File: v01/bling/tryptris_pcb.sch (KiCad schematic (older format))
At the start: 131 parts, among them J1 USB_C_Receptacle_USB2.0, J2 I2C-L, J3 I2C-R, SW1 Reset, U1 ATmega32U4-AU, U2 MCP23017_SO, Y1 16Mhz

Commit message: Use freeform routing to get USB ports in a better position.
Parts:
- J1, J2, J3: footprint Type-C:USB_C_GCT_USB4085 -> Connector_USB:USB_C_Receptacle_HRO_TYPE-C-31-M-12
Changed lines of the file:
@@
 F 0 "J1" H 5207 2517 50  0000 C CNN
 F 1 "USB_C_Receptacle_USB2.0" H 5207 2426 50  0000 C CNN
-F 2 "Type-C:USB_C_GCT_USB4085" H 5250 1650 50  0001 C CNN
+F 2 "Connector_USB:USB_C_Receptacle_HRO_TYPE-C-31-M-12" H 5250 1650 50  0001 C CNN
 F 3 "https://www.usb.org/sites/default/files/documents/usb_type-c.zip" H 5250 1650 50  0001 C CNN
 	1    5100 1650
@@
 F 0 "J2" H 5357 5917 50  0000 C CNN
 F 1 "I2C-L" H 5357 5826 50  0000 C CNN
-F 2 "Type-C:USB_C_GCT_USB4085" H 5400 5050 50  0001 C CNN
+F 2 "Connector_USB:USB_C_Receptacle_HRO_TYPE-C-31-M-12" H 5400 5050 50  0001 C CNN
 F 3 "https://www.usb.org/sites/default/files/documents/usb_type-c.zip" H 5400 5050 50  0001 C CNN
 	1    5250 5050
@@
 F 0 "J3" H 4907 8217 50  0000 C CNN
 F 1 "I2C-R" H 4907 8126 50  0000 C CNN
-F 2 "Type-C:USB_C_GCT_USB4085" H 4950 7350 50  0001 C CNN
+F 2 "Connector_USB:USB_C_Receptacle_HRO_TYPE-C-31-M-12" H 4950 7350 50  0001 C CNN
 F 3 "https://www.usb.org/sites/default/files/documents/usb_type-c.zip" H 4950 7350 50  0001 C CNN
 	1    4800 7350

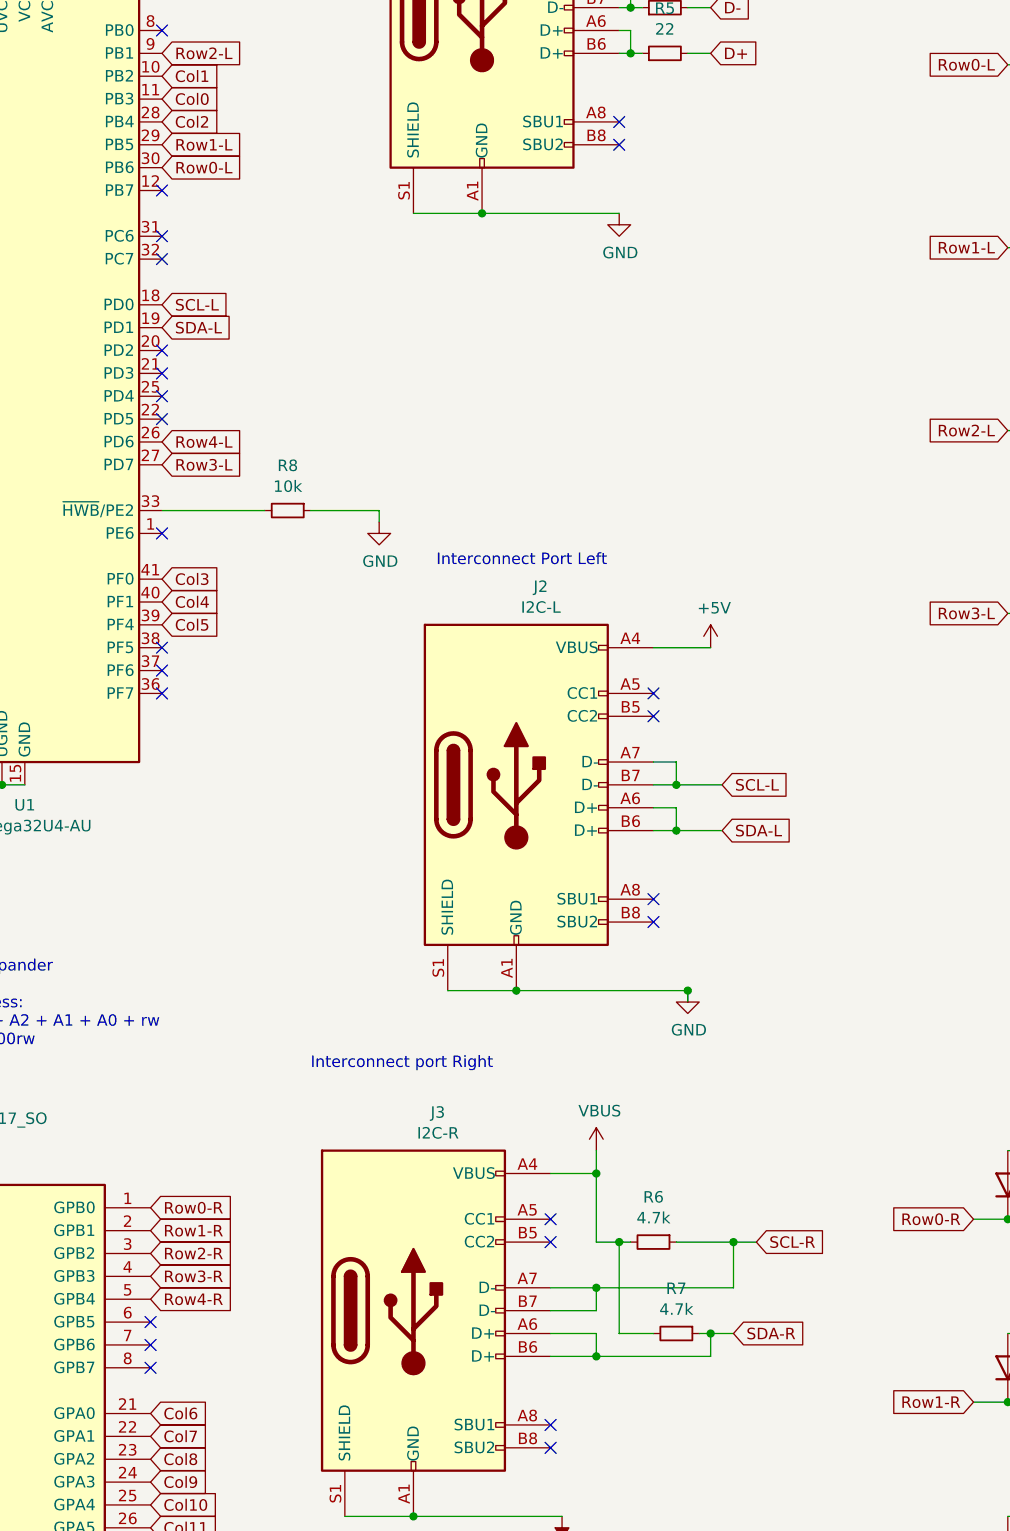
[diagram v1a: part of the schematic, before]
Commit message: Move I2C resistors to the left side for bling
This should ensure that the LED drivers on the left side work correctly
when the right side is not plugged in.
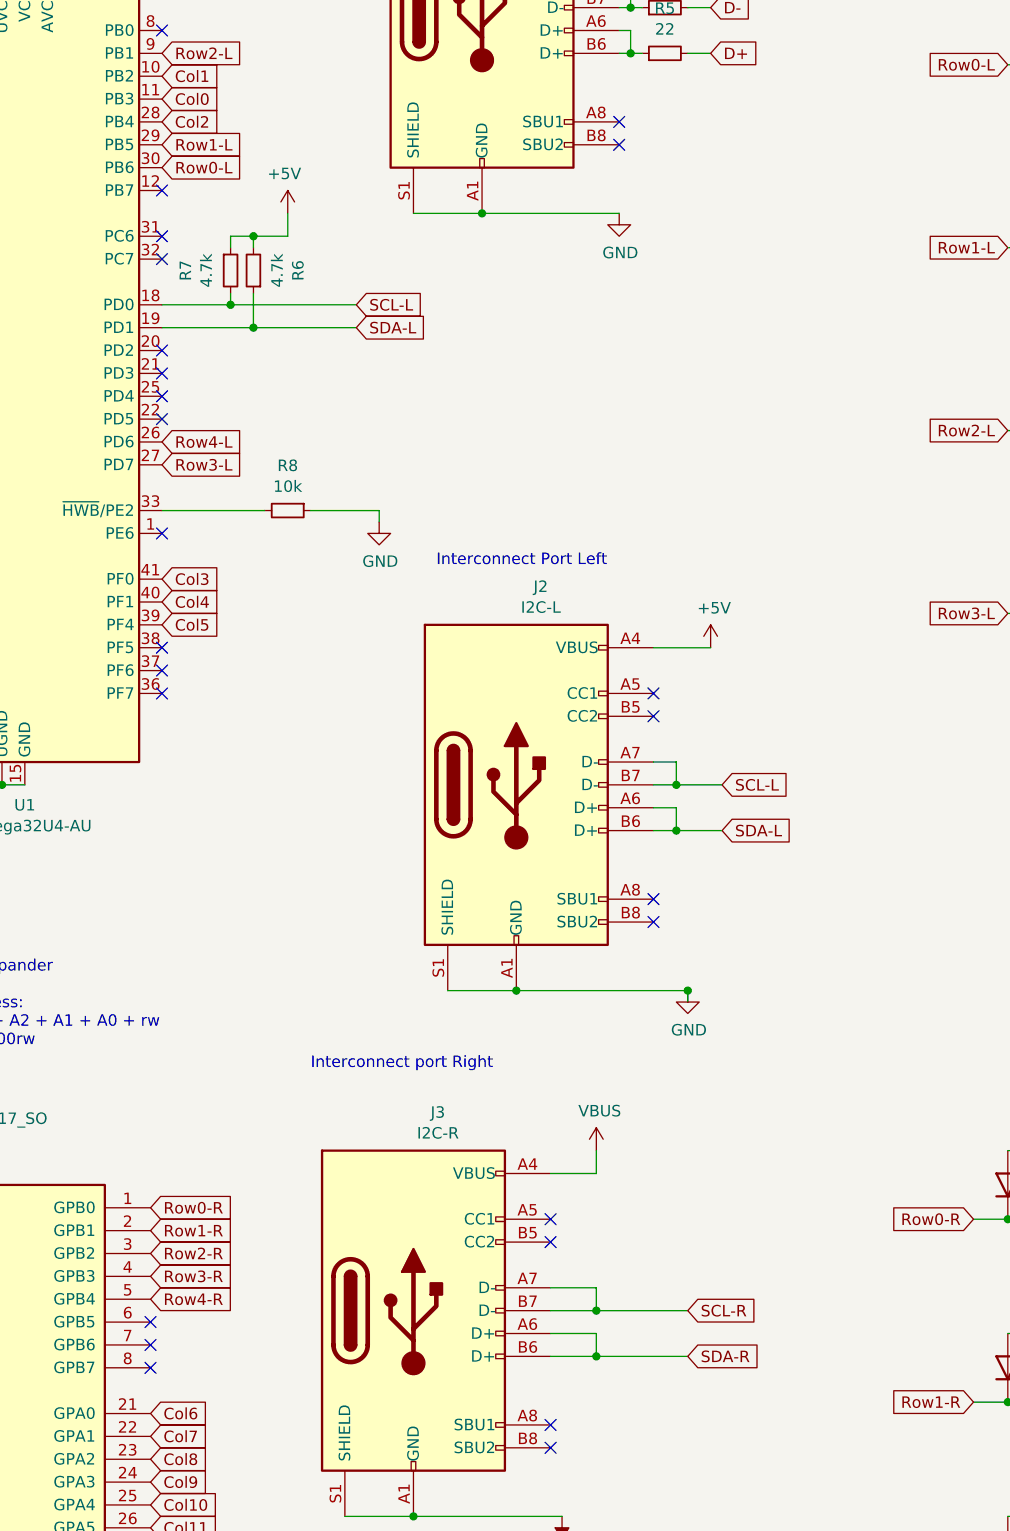
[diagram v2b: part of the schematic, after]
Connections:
- net +5V: now also R6.2, R7.1
- net SCL-L: now also R7.2
- net SCL-R: no longer R6.1
- net SDA-L: now also R6.1
- net SDA-R: no longer R7.1
- net VBUS: no longer R6.2, R7.2
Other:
- moved on the sheet: R6, R7
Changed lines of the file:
@@
 Text GLabel 2250 7000 0    50   Input ~ 0
 SCL-R
-Text GLabel 3700 3050 2    50   Input ~ 0
+Text GLabel 4550 3050 2    50   Input ~ 0
 SDA-L
-Text GLabel 3700 2950 2    50   Input ~ 0
+Text GLabel 4550 2950 2    50   Input ~ 0
 SCL-L
 Text Notes 4350 6300 0    50   ~ 0
@@
 Wire Wire Line
 	5600 6750 5600 6650
-Wire Wire Line
-	5600 7050 5700 7050
-Wire Wire Line
-	6200 7050 6300 7050
-Connection ~ 6200 7050
-Wire Wire Line
-	5950 7050 6200 7050
 $Comp
 L Device:R_Small R6
 U 1 1 615E83A9
-P 5850 7050
-F 0 "R6" V 5654 7050 50  0000 C CNN
-F 1 "4.7k" V 5745 7050 50  0000 C CNN
-F 2 "Resistor_SMD:R_0805_2012Metric" H 5850 7050 50  0001 C CNN
-F 3 "~" H 5850 7050 50  0001 C CNN
-	1    5850 7050
-	0    1    1    0
-$EndComp
-Text GLabel 6300 7050 2    50   Input ~ 0
+P 4100 2800
+F 0 "R6" V 3904 2800 50  0000 C CNN
+F 1 "4.7k" V 3995 2800 50  0000 C CNN
+F 2 "Resistor_SMD:R_0805_2012Metric" H 4100 2800 50  0001 C CNN
+F 3 "~" H 4100 2800 50  0001 C CNN
+	1    4100 2800
+	-1   0    0    1
+$EndComp
+Text GLabel 6000 7350 2    50   Input ~ 0
 SCL-R
-Wire Wire Line
-	5600 7250 6200 7250
-Wire Wire Line
-	6200 7050 6200 7250
-Connection ~ 5600 7250
-Wire Wire Line
-	5600 6750 5600 7050
-Connection ~ 5600 6750
-Wire Wire Line
-	6100 7450 6200 7450
-Connection ~ 6100 7450
-Wire Wire Line
-	6100 7550 6100 7450
-Wire Wire Line
-	6050 7450 6100 7450
-$Comp
-L Device:R_Small R7
-U 1 1 61698CA9
-P 5950 7450
-F 0 "R7" V 5754 7450 50  0000 C CNN
-F 1 "4.7k" V 5845 7450 50  0000 C CNN
-F 2 "Resistor_SMD:R_0805_2012Metric" H 5950 7450 50  0001 C CNN
-F 3 "~" H 5950 7450 50  0001 C CNN
-	1    5950 7450
-	0    1    1    0
-$EndComp
-Text GLabel 6200 7450 2    50   Input ~ 0
+Text GLabel 6000 7550 2    50   Input ~ 0
 SDA-R
-Wire Wire Line
-	5600 7550 6100 7550
-Connection ~ 5600 7550
-Wire Wire Line
-	5700 7050 5700 7450
-Wire Wire Line
-	5700 7450 5850 7450
-Connection ~ 5700 7050
-Wire Wire Line
-	5700 7050 5750 7050
 NoConn ~ 5850 5550
 NoConn ~ 5850 5650
@@
 F1 "rgb matrix.sch" 50
 $EndSheet
+Wire Wire Line
+	5600 7350 6000 7350
+Connection ~ 5600 7350
+Wire Wire Line
+	5600 7550 6000 7550
+Connection ~ 5600 7550
+$Comp
+L Device:R_Small R7
+U 1 1 61698CA9
+P 4000 2800
+F 0 "R7" V 3804 2800 50  0000 C CNN
+F 1 "4.7k" V 3895 2800 50  0000 C CNN
+F 2 "Resistor_SMD:R_0805_2012Metric" H 4000 2800 50  0001 C CNN
+F 3 "~" H 4000 2800 50  0001 C CNN
+	1    4000 2800
+	1    0    0    -1
+$EndComp
+$Comp
+L power:+5V #PWR0150
+U 1 1 61876A22
+P 4250 2550
+F 0 "#PWR0150" H 4250 2400 50  0001 C CNN
+F 1 "+5V" H 4265 2723 50  0000 C CNN
+F 2 "" H 4250 2550 50  0001 C CNN
+F 3 "" H 4250 2550 50  0001 C CNN
+	1    4250 2550
+	-1   0    0    -1
+$EndComp
+Wire Wire Line
+	4250 2550 4250 2650
+Wire Wire Line
+	4250 2650 4100 2650
+Wire Wire Line
+	4000 2650 4000 2700
+Wire Wire Line
+	4100 2650 4100 2700
+Connection ~ 4100 2650
+Wire Wire Line
+	4100 2650 4000 2650
+Wire Wire Line
+	3700 2950 4000 2950
+Wire Wire Line
+	4000 2900 4000 2950
+Connection ~ 4000 2950
+Wire Wire Line
+	4000 2950 4550 2950
+Wire Wire Line
+	3700 3050 4100 3050
+Wire Wire Line
+	4100 2900 4100 3050
+Connection ~ 4100 3050
+Wire Wire Line
+	4100 3050 4550 3050
 $EndSCHEMATC

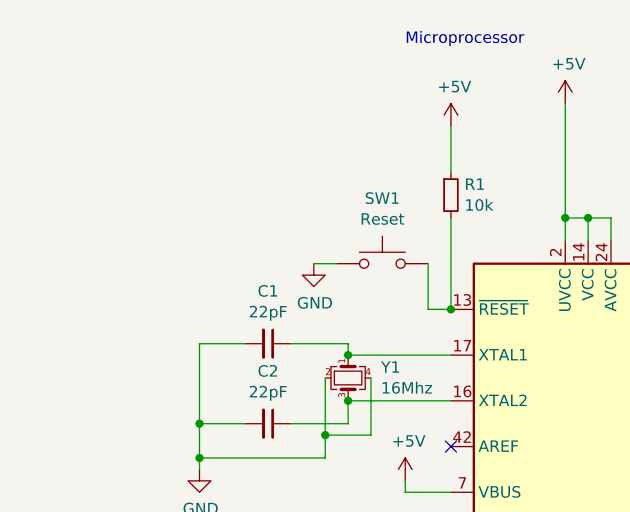
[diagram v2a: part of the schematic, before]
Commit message: Add ISP port to the bling board.
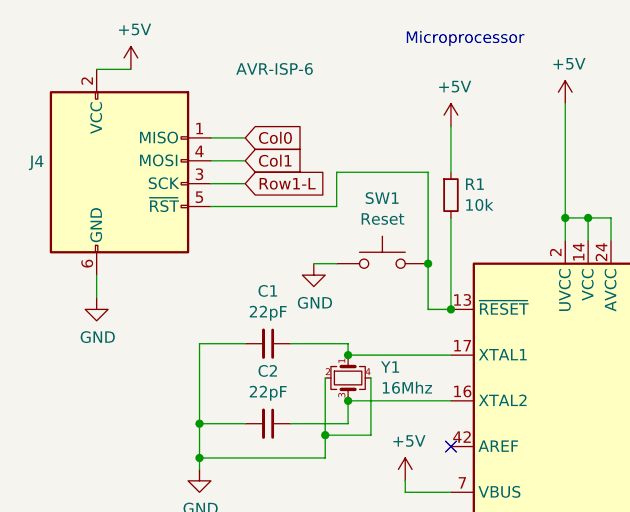
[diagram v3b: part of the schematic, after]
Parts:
- added J4: AVR-ISP-6, random-keyboard-parts:Reset_Pretty-Mask, symbol Connector:AVR-ISP-6
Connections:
- net +5V: now also J4.2 (VCC)
- net Col0: now also J4.1 (MISO)
- net Col1: now also J4.4 (MOSI)
- net GND: now also J4.6 (GND)
- net Row1-L: now also J4.3 (SCK)
- net at R1.2, SW1.2, U1.13 (~RESET): now also J4.5 (~RST)
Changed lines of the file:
@@
 Text GLabel 3700 2350 2    50   Input ~ 0
 Row0-L
-Text GLabel 3700 2250 2    50   Input ~ 0
-Row1-L
 Text GLabel 3700 1850 2    50   Input ~ 0
 Row2-L
@@
 Text GLabel 3700 1950 2    50   Input ~ 0
 Col1
-Text GLabel 3700 2150 2    50   Input ~ 0
-Col2
 Text GLabel 3700 4150 2    50   Input ~ 0
 Col3
@@
 Wire Wire Line
 	4100 3050 4550 3050
+$Comp
+L Connector:AVR-ISP-6 J4
+U 1 1 614FA457
+P 1050 1200
+F 0 "J4" H 721 1296 50  0000 R CNN
+F 1 "AVR-ISP-6" H 1900 1700 50  0000 R CNN
+F 2 "random-keyboard-parts:Reset_Pretty-Mask" V 800 1250 50  0001 C CNN
+F 3 " ~" H -225 650 50  0001 C CNN
+	1    1050 1200
+	1    0    0    -1
+$EndComp
+$Comp
+L power:+5V #PWR0151
+U 1 1 614FC032
+P 1100 700
+F 0 "#PWR0151" H 1100 550 50  0001 C CNN
+F 1 "+5V" H 1115 873 50  0000 C CNN
+F 2 "" H 1100 700 50  0001 C CNN
+F 3 "" H 1100 700 50  0001 C CNN
+	1    1100 700
+	1    0    0    -1
+$EndComp
+Wire Wire Line
+	1100 700  950  700
+$Comp
+L power:GND #PWR0152
+U 1 1 615164A9
+P 950 1700
+F 0 "#PWR0152" H 950 1450 50  0001 C CNN
+F 1 "GND" H 955 1527 50  0000 C CNN
+F 2 "" H 950 1700 50  0001 C CNN
+F 3 "" H 950 1700 50  0001 C CNN
+	1    950  1700
+	1    0    0    -1
+$EndComp
+Wire Wire Line
+	950  1700 950  1600
+Text GLabel 1600 1000 2    50   Input ~ 0
+Col0
+Wire Wire Line
+	1600 1000 1450 1000
+Text GLabel 1600 1100 2    50   Input ~ 0
+Col1
+Wire Wire Line
+	1600 1100 1450 1100
+Text GLabel 1600 1200 2    50   Input ~ 0
+Row1-L
+Wire Wire Line
+	1600 1200 1450 1200
+Wire Wire Line
+	1450 1300 2000 1300
+Wire Wire Line
+	2000 1300 2000 1150
+Wire Wire Line
+	2000 1150 2400 1150
+Wire Wire Line
+	2400 1150 2400 1550
+Connection ~ 2400 1550
+Text GLabel 3700 2150 2    50   Input ~ 0
+Col2
+Text GLabel 3700 2250 2    50   Input ~ 0
+Row1-L
 $EndSCHEMATC

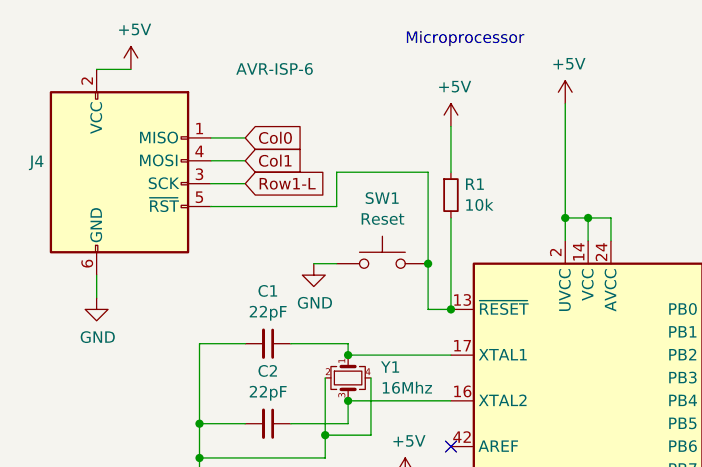
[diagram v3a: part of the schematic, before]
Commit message: Fix ISP connection and move mounting holes
I had the pins wrong. Top mounting holes are more equal in height and
evenly spread around the board.
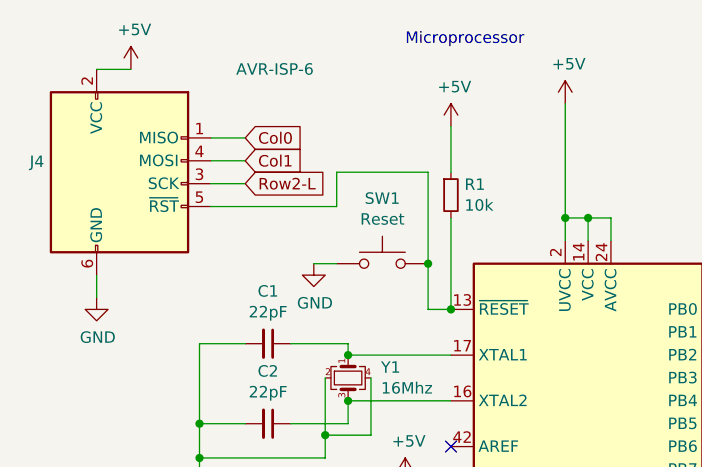
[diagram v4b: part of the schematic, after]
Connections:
- net Row1-L: no longer J4.3 (SCK)
- net Row2-L: now also J4.3 (SCK)
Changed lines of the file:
@@
 	1600 1100 1450 1100
 Text GLabel 1600 1200 2    50   Input ~ 0
-Row1-L
+Row2-L
 Wire Wire Line
 	1600 1200 1450 1200

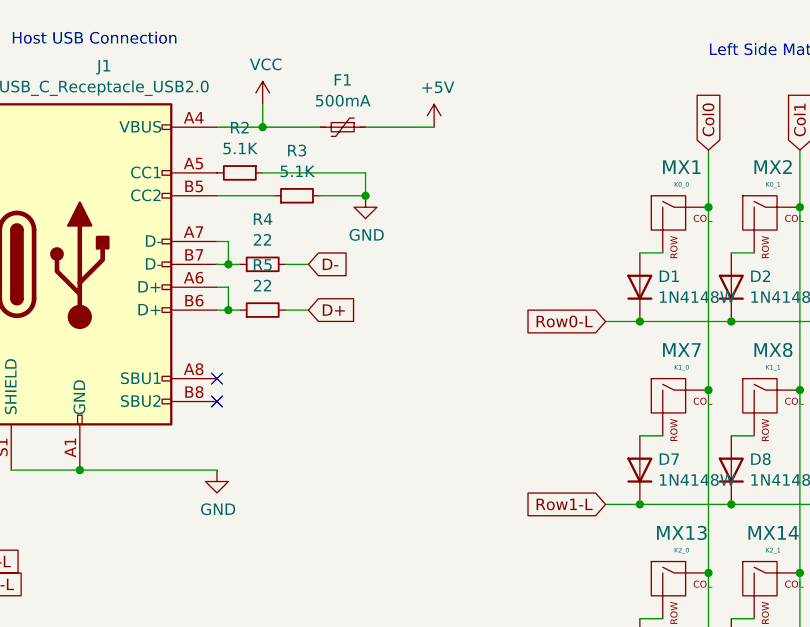
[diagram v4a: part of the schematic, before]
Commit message: Add ESD component to both boards.
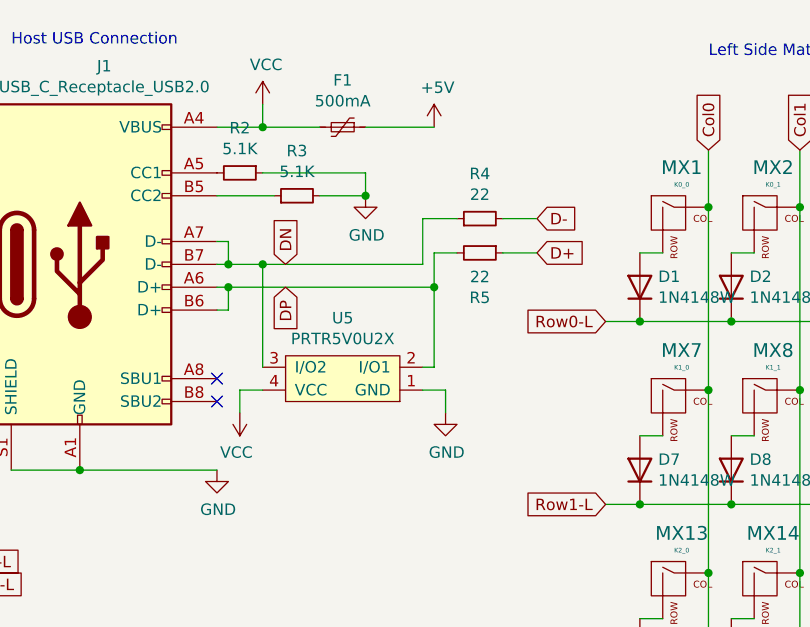
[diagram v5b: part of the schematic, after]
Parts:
- added U5: PRTR5V0U2X, Keebio-Parts:SOT-143B, symbol keebio:PRTR5V0U2X
- F1: footprint Fuse:Fuse_0805_2012Metric_Pad1.15x1.40mm_HandSolder -> Fuse:Fuse_1206_3216Metric_Pad1.42x1.75mm_HandSolder
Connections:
- net D+: now also R5.1; no longer R5.2
- net GND: now also U5.1 (GND)
- net VCC: now also U5.4 (VCC)
- net DP: now reaches J1.A6 (D+), J1.B6 (D+)
- net DP: now also R5.2, U5.2 (I/O1); no longer R5.1
- net DN: now reaches J1.A7 (D-), J1.B7 (D-), R4.1
- net DN: now also U5.3 (I/O2)
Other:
- moved on the sheet: R4, R5
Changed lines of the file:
@@
 F 0 "F1" V 6045 1050 50  0000 C CNN
 F 1 "500mA" V 6136 1050 50  0000 C CNN
-F 2 "Fuse:Fuse_0805_2012Metric_Pad1.15x1.40mm_HandSolder" H 6300 850 50  0001 L CNN
+F 2 "Fuse:Fuse_1206_3216Metric_Pad1.42x1.75mm_HandSolder" H 6300 850 50  0001 L CNN
 F 3 "~" H 6250 1050 50  0001 C CNN
 	1    6250 1050
@@
 L Device:R_Small R4
 U 1 1 61EF46E6
-P 5900 1650
-F 0 "R4" V 6096 1650 50  0000 C CNN
-F 1 "22" V 6005 1650 50  0000 C CNN
-F 2 "Resistor_SMD:R_0805_2012Metric" H 5900 1650 50  0001 C CNN
-F 3 "~" H 5900 1650 50  0001 C CNN
-	1    5900 1650
+P 6850 1450
+F 0 "R4" V 7046 1450 50  0000 C CNN
+F 1 "22" V 6955 1450 50  0000 C CNN
+F 2 "Resistor_SMD:R_0805_2012Metric" H 6850 1450 50  0001 C CNN
+F 3 "~" H 6850 1450 50  0001 C CNN
+	1    6850 1450
 	0    -1   -1   0
 $EndComp
@@
 	5750 1550 5750 1650
 Connection ~ 5750 1650
-Wire Wire Line
-	5750 1650 5800 1650
-Text GLabel 6100 1650 2    50   Input ~ 0
+Text GLabel 7100 1450 2    50   Input ~ 0
 D-
 Wire Wire Line
-	6000 1650 6100 1650
-$Comp
-L Device:R_Small R5
-U 1 1 61F3054F
-P 5900 1850
-F 0 "R5" V 6096 1850 50  0000 C CNN
-F 1 "22" V 6005 1850 50  0000 C CNN
-F 2 "Resistor_SMD:R_0805_2012Metric" H 5900 1850 50  0001 C CNN
-F 3 "~" H 5900 1850 50  0001 C CNN
-	1    5900 1850
-	0    -1   -1   0
-$EndComp
-Wire Wire Line
 	5700 1850 5750 1850
 Wire Wire Line
 	5700 1750 5750 1750
-Wire Wire Line
-	5750 1750 5750 1850
-Connection ~ 5750 1850
-Wire Wire Line
-	5750 1850 5800 1850
-Text GLabel 6100 1850 2    50   Input ~ 0
+Text GLabel 7100 1600 2    50   Input ~ 0
 D+
-Wire Wire Line
-	6000 1850 6100 1850
 NoConn ~ 5700 2150
 NoConn ~ 5700 2250
@@
 Text GLabel 3700 2250 2    50   Input ~ 0
 Row1-L
+$Comp
+L Device:R_Small R5
+U 1 1 61F3054F
+P 6850 1600
+F 0 "R5" V 7046 1600 50  0000 C CNN
+F 1 "22" V 6955 1600 50  0000 C CNN
+F 2 "Resistor_SMD:R_0805_2012Metric" H 6850 1600 50  0001 C CNN
+F 3 "~" H 6850 1600 50  0001 C CNN
+	1    6850 1600
+	0    1    1    0
+$EndComp
+$Comp
+L keebio:PRTR5V0U2X U5
+U 1 1 6185F515
+P 6250 2150
+F 0 "U5" H 6250 1885 50  0000 C CNN
+F 1 "PRTR5V0U2X" H 6250 1976 50  0000 C CNN
+F 2 "Keebio-Parts:SOT-143B" H 6200 2250 50  0001 C CNN
+F 3 "" H 6200 2250 50  0001 C CNN
+	1    6250 2150
+	-1   0    0    1
+$EndComp
+$Comp
+L power:VCC #PWR0153
+U 1 1 618D0527
+P 5800 2300
+F 0 "#PWR0153" H 5800 2150 50  0001 C CNN
+F 1 "VCC" H 5815 2473 50  0000 C CNN
+F 2 "" H 5800 2300 50  0001 C CNN
+F 3 "" H 5800 2300 50  0001 C CNN
+	1    5800 2300
+	-1   0    0    1
+$EndComp
+Wire Wire Line
+	5900 2200 5800 2200
+Wire Wire Line
+	5800 2200 5800 2300
+$Comp
+L power:GND #PWR0154
+U 1 1 618EC898
+P 6700 2300
+F 0 "#PWR0154" H 6700 2050 50  0001 C CNN
+F 1 "GND" H 6705 2127 50  0000 C CNN
+F 2 "" H 6700 2300 50  0001 C CNN
+F 3 "" H 6700 2300 50  0001 C CNN
+	1    6700 2300
+	1    0    0    -1
+$EndComp
+Wire Wire Line
+	6700 2300 6700 2200
+Wire Wire Line
+	6700 2200 6600 2200
+Wire Wire Line
+	7100 1600 6950 1600
+Wire Wire Line
+	7100 1450 6950 1450
+Wire Wire Line
+	6650 1600 6750 1600
+Wire Wire Line
+	5750 1750 5750 1850
+Connection ~ 5750 1750
+Wire Wire Line
+	6650 1600 6650 1750
+Wire Wire Line
+	6600 1450 6750 1450
+Wire Wire Line
+	6600 1450 6600 1650
+Wire Wire Line
+	5750 1650 5900 1650
+Text GLabel 6000 1650 1    50   Input ~ 0
+DN
+Text GLabel 6000 1750 3    50   Input ~ 0
+DP
+Wire Wire Line
+	5750 1750 6650 1750
+Wire Wire Line
+	5900 2100 5900 1650
+Connection ~ 5900 1650
+Wire Wire Line
+	5900 1650 6600 1650
+Wire Wire Line
+	6600 2100 6650 2100
+Wire Wire Line
+	6650 2100 6650 1750
+Connection ~ 6650 1750
 $EndSCHEMATC
